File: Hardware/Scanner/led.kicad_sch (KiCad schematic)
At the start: 20 parts, among them U5 TLC59208FIPWR

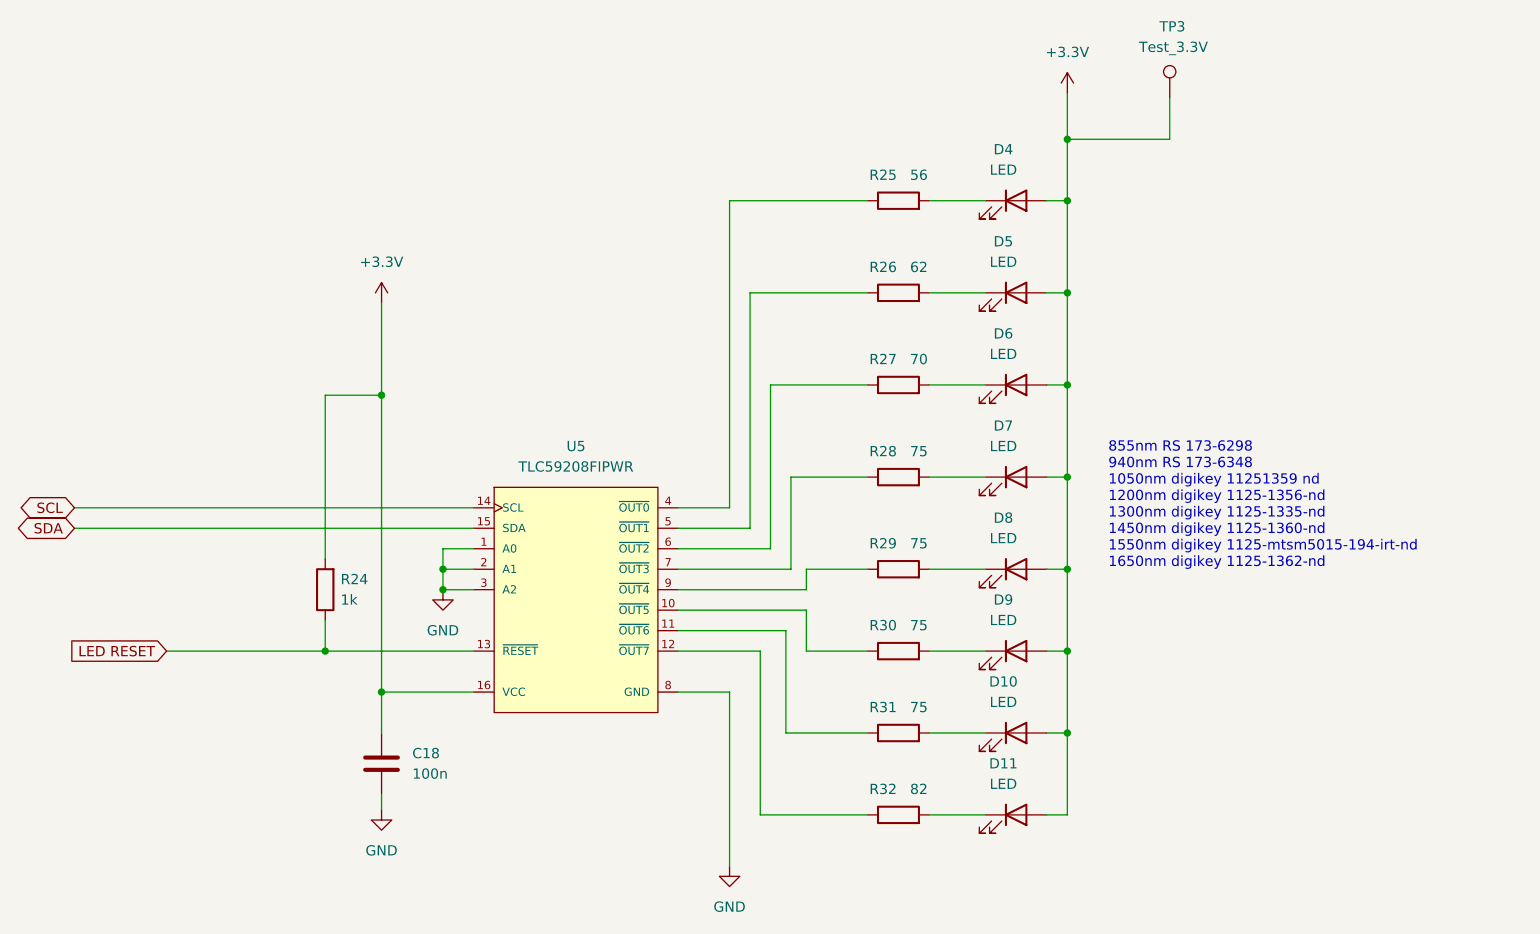
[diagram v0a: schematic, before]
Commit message: Updated LED and crystal descriptions
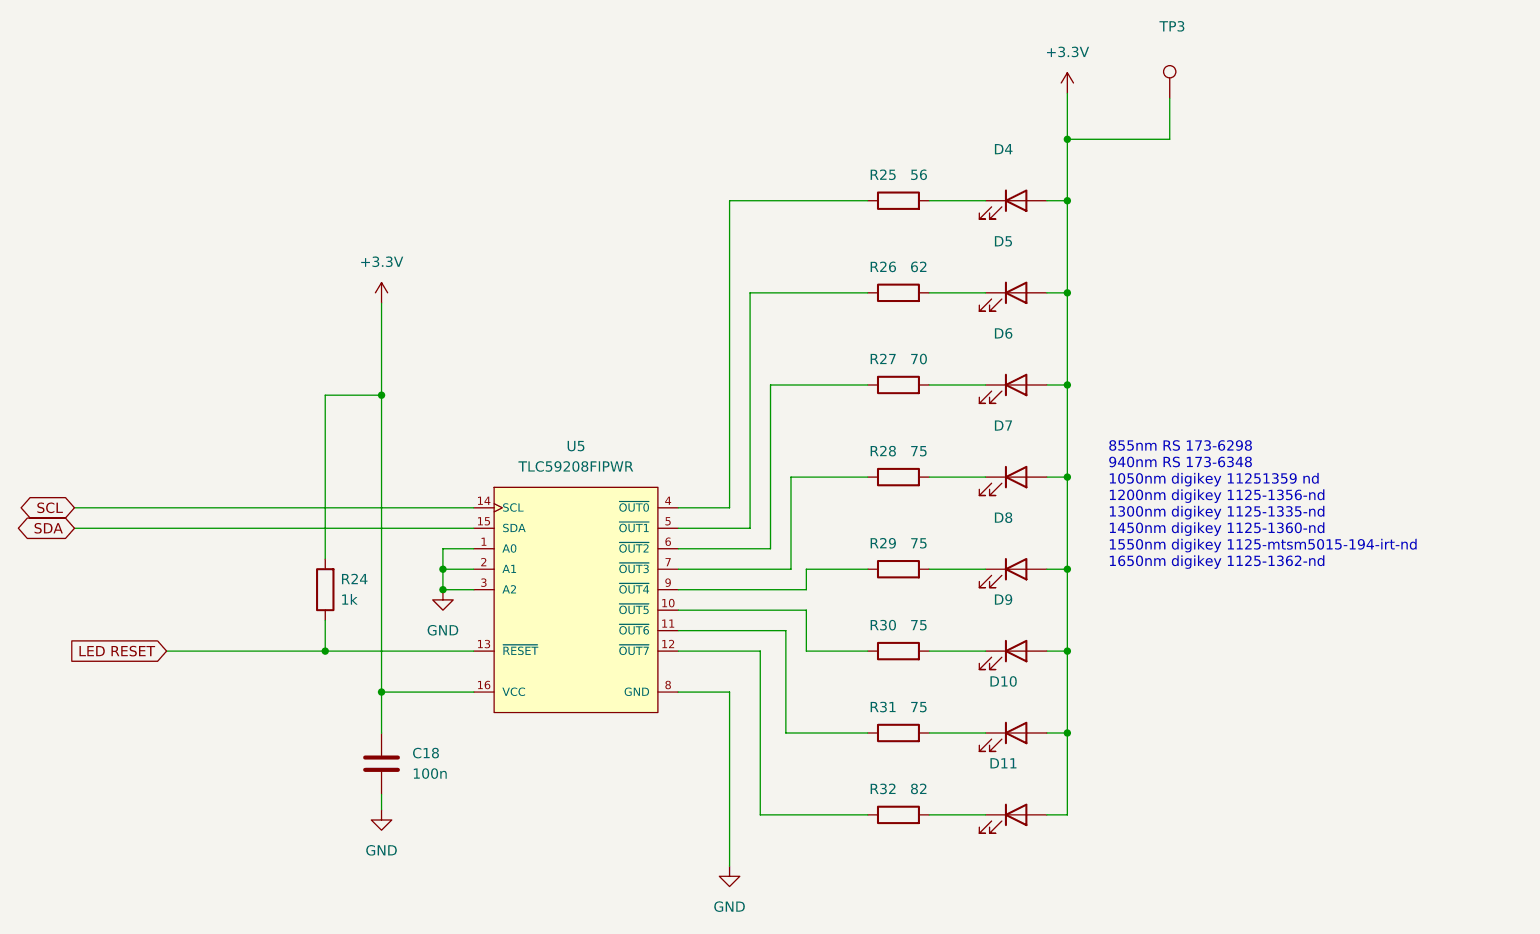
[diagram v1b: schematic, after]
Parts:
- D10, D11, D4, D5, D6, D7, D8, D9: value LED -> (none); footprint LED_SMD:LED_1206_3216Metric_Pad1.42x1.75mm_HandSolder -> (none)
- TP3: value Test_3.3V -> (none); footprint TestPoint:TestPoint_Pad_D1.5mm -> (none); now left out of the parts list
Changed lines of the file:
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@@
     (in_bom yes) (on_board yes) (fields_autoplaced)
     (property "Reference" "D8" (id 0) (at 200.3425 93.98 0))
-    (property "Value" "LED" (id 1) (at 200.3425 96.52 0))
-    (property "Footprint" "LED_SMD:LED_1206_3216Metric_Pad1.42x1.75mm_HandSolder" (id 2) (at 201.93 100.33 0)
+    (property "Value" "" (id 1) (at 200.3425 96.52 0))
+    (property "Footprint" "" (id 2) (at 201.93 100.33 0)
       (effects (font (size 1.27 1.27)) hide)
     )
@@
   )
   (symbol (lib_id "Connector:TestPoint") (at 220.98 41.91 0) (unit 1)
-    (in_bom yes) (on_board yes)
+    (in_bom no) (on_board yes)
     (property "Reference" "TP3" (id 0) (at 219.71 33.02 0)
       (effects (font (size 1.27 1.27)) (justify left))
     )
-    (property "Value" "Test_3.3V" (id 1) (at 217.17 35.56 0)
+    (property "Value" "" (id 1) (at 217.17 35.56 0)
       (effects (font (size 1.27 1.27)) (justify left))
     )
-    (property "Footprint" "TestPoint:TestPoint_Pad_D1.5mm" (id 2) (at 226.06 41.91 0)
+    (property "Footprint" "" (id 2) (at 226.06 41.91 0)
       (effects (font (size 1.27 1.27)) hide)
     )
@@
     (in_bom yes) (on_board yes) (fields_autoplaced)
     (property "Reference" "D9" (id 0) (at 200.3425 104.14 0))
-    (property "Value" "LED" (id 1) (at 200.3425 106.68 0))
-    (property "Footprint" "LED_SMD:LED_1206_3216Metric_Pad1.42x1.75mm_HandSolder" (id 2) (at 201.93 110.49 0)
+    (property "Value" "" (id 1) (at 200.3425 106.68 0))
+    (property "Footprint" "" (id 2) (at 201.93 110.49 0)
       (effects (font (size 1.27 1.27)) hide)
     )
@@
     (in_bom yes) (on_board yes) (fields_autoplaced)
     (property "Reference" "D4" (id 0) (at 200.3425 48.26 0))
-    (property "Value" "LED" (id 1) (at 200.3425 50.8 0))
-    (property "Footprint" "LED_SMD:LED_1206_3216Metric_Pad1.42x1.75mm_HandSolder" (id 2) (at 201.93 54.61 0)
+    (property "Value" "" (id 1) (at 200.3425 50.8 0))
+    (property "Footprint" "" (id 2) (at 201.93 54.61 0)
       (effects (font (size 1.27 1.27)) hide)
     )
@@
     (in_bom yes) (on_board yes) (fields_autoplaced)
     (property "Reference" "D7" (id 0) (at 200.3425 82.55 0))
-    (property "Value" "LED" (id 1) (at 200.3425 85.09 0))
-    (property "Footprint" "LED_SMD:LED_1206_3216Metric_Pad1.42x1.75mm_HandSolder" (id 2) (at 201.93 88.9 0)
+    (property "Value" "" (id 1) (at 200.3425 85.09 0))
+    (property "Footprint" "" (id 2) (at 201.93 88.9 0)
       (effects (font (size 1.27 1.27)) hide)
     )
@@
     (in_bom yes) (on_board yes) (fields_autoplaced)
     (property "Reference" "D11" (id 0) (at 200.3425 124.46 0))
-    (property "Value" "LED" (id 1) (at 200.3425 127 0))
-    (property "Footprint" "LED_SMD:LED_1206_3216Metric_Pad1.42x1.75mm_HandSolder" (id 2) (at 201.93 130.81 0)
+    (property "Value" "" (id 1) (at 200.3425 127 0))
+    (property "Footprint" "" (id 2) (at 201.93 130.81 0)
       (effects (font (size 1.27 1.27)) hide)
     )
@@
     (in_bom yes) (on_board yes) (fields_autoplaced)
     (property "Reference" "D6" (id 0) (at 200.3425 71.12 0))
-    (property "Value" "LED" (id 1) (at 200.3425 73.66 0))
-    (property "Footprint" "LED_SMD:LED_1206_3216Metric_Pad1.42x1.75mm_HandSolder" (id 2) (at 201.93 77.47 0)
+    (property "Value" "" (id 1) (at 200.3425 73.66 0))
+    (property "Footprint" "" (id 2) (at 201.93 77.47 0)
       (effects (font (size 1.27 1.27)) hide)
     )
@@
     (in_bom yes) (on_board yes) (fields_autoplaced)
     (property "Reference" "D5" (id 0) (at 200.3425 59.69 0))
-    (property "Value" "LED" (id 1) (at 200.3425 62.23 0))
-    (property "Footprint" "LED_SMD:LED_1206_3216Metric_Pad1.42x1.75mm_HandSolder" (id 2) (at 201.93 66.04 0)
+    (property "Value" "" (id 1) (at 200.3425 62.23 0))
+    (property "Footprint" "" (id 2) (at 201.93 66.04 0)
       (effects (font (size 1.27 1.27)) hide)
     )
@@
     (in_bom yes) (on_board yes) (fields_autoplaced)
     (property "Reference" "D10" (id 0) (at 200.3425 114.3 0))
-    (property "Value" "LED" (id 1) (at 200.3425 116.84 0))
-    (property "Footprint" "LED_SMD:LED_1206_3216Metric_Pad1.42x1.75mm_HandSolder" (id 2) (at 201.93 120.65 0)
-      (effects (font (size 1.27 1.27)) hide)
-    )
+    (property "Value" "" (id 1) (at 200.3425 116.84 0))
+    (property "Footprint" "" (id 2) (at 201.93 120.65 0)
+      (effects (font (size 1.27 1.27)) hide)
+    )

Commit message: Consistency of capacitor values
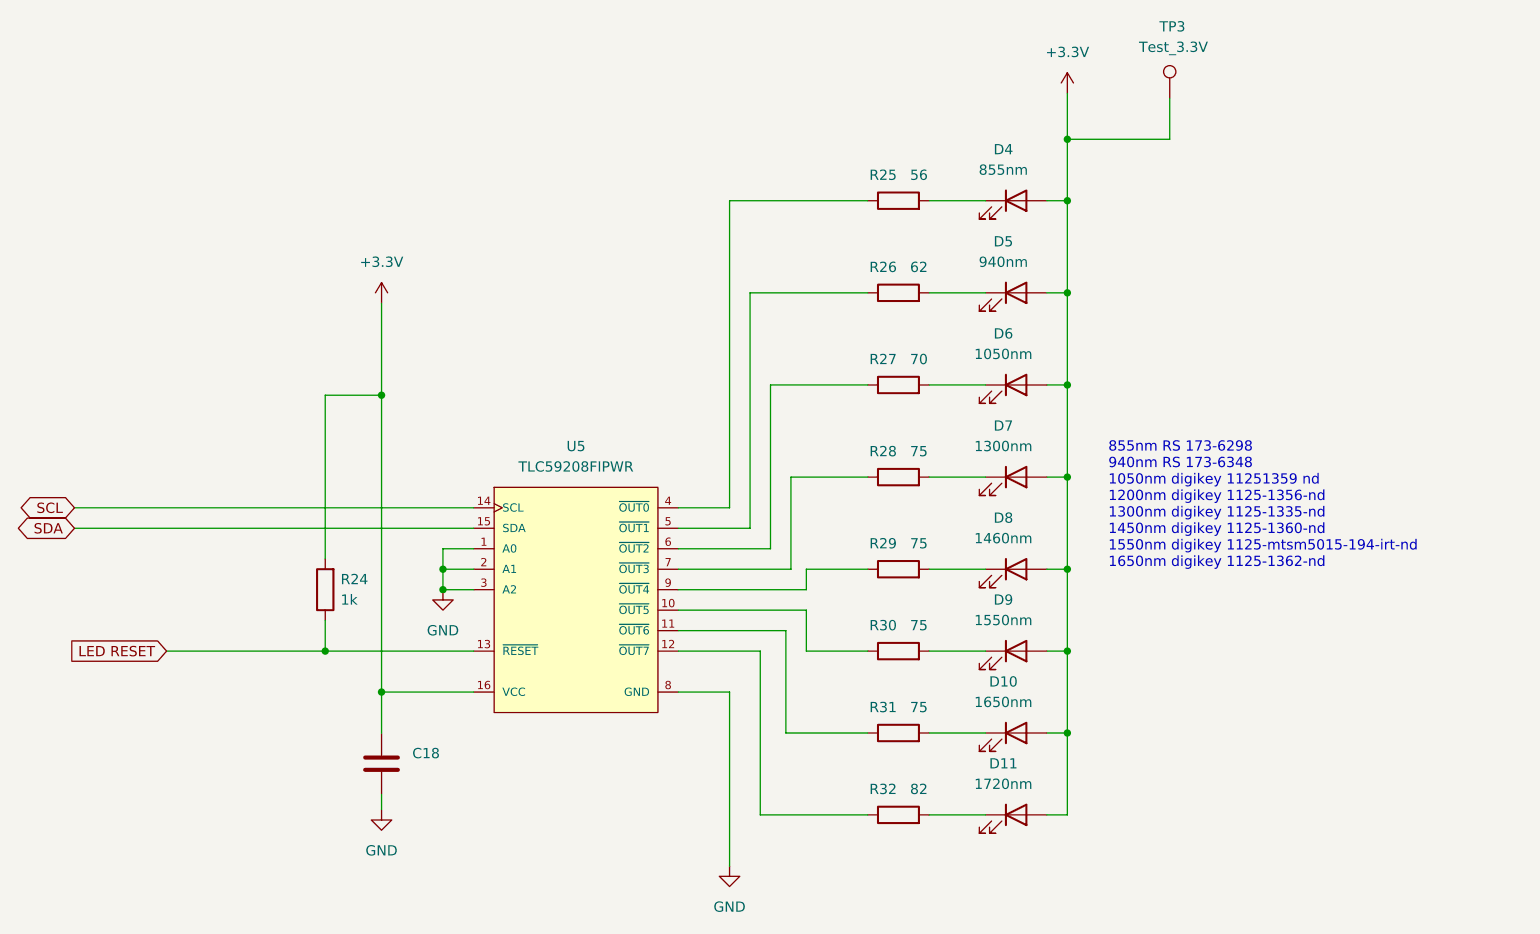
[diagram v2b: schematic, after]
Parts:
- C18: value 100n -> (none)
- D10: value (none) -> 1650nm; footprint (none) -> LED_SMD:LED_1206_3216Metric_Pad1.42x1.75mm_HandSolder
- D11: value (none) -> 1720nm; footprint (none) -> LED_SMD:LED_1206_3216Metric_Pad1.42x1.75mm_HandSolder
- D4: value (none) -> 855nm; footprint (none) -> LED_SMD:LED_1206_3216Metric_Pad1.42x1.75mm_HandSolder
- D5: value (none) -> 940nm; footprint (none) -> LED_SMD:LED_1206_3216Metric_Pad1.42x1.75mm_HandSolder
- D6: value (none) -> 1050nm; footprint (none) -> LED_SMD:LED_1206_3216Metric_Pad1.42x1.75mm_HandSolder
- D7: value (none) -> 1300nm; footprint (none) -> LED_SMD:LED_1206_3216Metric_Pad1.42x1.75mm_HandSolder
- D8: value (none) -> 1460nm; footprint (none) -> LED_SMD:LED_1206_3216Metric_Pad1.42x1.75mm_HandSolder
- D9: value (none) -> 1550nm; footprint (none) -> LED_SMD:LED_1206_3216Metric_Pad1.42x1.75mm_HandSolder
- TP3: value (none) -> Test_3.3V; footprint (none) -> TestPoint:TestPoint_Pad_D1.5mm
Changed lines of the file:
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@@
     (in_bom yes) (on_board yes) (fields_autoplaced)
     (property "Reference" "D8" (id 0) (at 200.3425 93.98 0))
-    (property "Value" "" (id 1) (at 200.3425 96.52 0))
-    (property "Footprint" "" (id 2) (at 201.93 100.33 0)
+    (property "Value" "1460nm" (id 1) (at 200.3425 96.52 0))
+    (property "Footprint" "LED_SMD:LED_1206_3216Metric_Pad1.42x1.75mm_HandSolder" (id 2) (at 201.93 100.33 0)
       (effects (font (size 1.27 1.27)) hide)
     )
@@
       (effects (font (size 1.27 1.27)) (justify left))
     )
-    (property "Value" "" (id 1) (at 217.17 35.56 0)
+    (property "Value" "Test_3.3V" (id 1) (at 217.17 35.56 0)
       (effects (font (size 1.27 1.27)) (justify left))
     )
-    (property "Footprint" "" (id 2) (at 226.06 41.91 0)
+    (property "Footprint" "TestPoint:TestPoint_Pad_D1.5mm" (id 2) (at 226.06 41.91 0)
       (effects (font (size 1.27 1.27)) hide)
     )
@@
       (effects (font (size 1.27 1.27)) (justify left))
     )
-    (property "Value" "100n" (id 1) (at 127 125.7299 0)
+    (property "Value" "" (id 1) (at 127 125.7299 0)
       (effects (font (size 1.27 1.27)) (justify left))
     )
@@
     (in_bom yes) (on_board yes) (fields_autoplaced)
     (property "Reference" "D9" (id 0) (at 200.3425 104.14 0))
-    (property "Value" "" (id 1) (at 200.3425 106.68 0))
-    (property "Footprint" "" (id 2) (at 201.93 110.49 0)
+    (property "Value" "1550nm" (id 1) (at 200.3425 106.68 0))
+    (property "Footprint" "LED_SMD:LED_1206_3216Metric_Pad1.42x1.75mm_HandSolder" (id 2) (at 201.93 110.49 0)
       (effects (font (size 1.27 1.27)) hide)
     )
@@
     (in_bom yes) (on_board yes) (fields_autoplaced)
     (property "Reference" "D4" (id 0) (at 200.3425 48.26 0))
-    (property "Value" "" (id 1) (at 200.3425 50.8 0))
-    (property "Footprint" "" (id 2) (at 201.93 54.61 0)
+    (property "Value" "855nm " (id 1) (at 200.3425 50.8 0))
+    (property "Footprint" "LED_SMD:LED_1206_3216Metric_Pad1.42x1.75mm_HandSolder" (id 2) (at 201.93 54.61 0)
       (effects (font (size 1.27 1.27)) hide)
     )
@@
     (in_bom yes) (on_board yes) (fields_autoplaced)
     (property "Reference" "D7" (id 0) (at 200.3425 82.55 0))
-    (property "Value" "" (id 1) (at 200.3425 85.09 0))
-    (property "Footprint" "" (id 2) (at 201.93 88.9 0)
+    (property "Value" "1300nm" (id 1) (at 200.3425 85.09 0))
+    (property "Footprint" "LED_SMD:LED_1206_3216Metric_Pad1.42x1.75mm_HandSolder" (id 2) (at 201.93 88.9 0)
       (effects (font (size 1.27 1.27)) hide)
     )
@@
     (in_bom yes) (on_board yes) (fields_autoplaced)
     (property "Reference" "D11" (id 0) (at 200.3425 124.46 0))
-    (property "Value" "" (id 1) (at 200.3425 127 0))
-    (property "Footprint" "" (id 2) (at 201.93 130.81 0)
+    (property "Value" "1720nm" (id 1) (at 200.3425 127 0))
+    (property "Footprint" "LED_SMD:LED_1206_3216Metric_Pad1.42x1.75mm_HandSolder" (id 2) (at 201.93 130.81 0)
       (effects (font (size 1.27 1.27)) hide)
     )
@@
     (in_bom yes) (on_board yes) (fields_autoplaced)
     (property "Reference" "D6" (id 0) (at 200.3425 71.12 0))
-    (property "Value" "" (id 1) (at 200.3425 73.66 0))
-    (property "Footprint" "" (id 2) (at 201.93 77.47 0)
+    (property "Value" "1050nm" (id 1) (at 200.3425 73.66 0))
+    (property "Footprint" "LED_SMD:LED_1206_3216Metric_Pad1.42x1.75mm_HandSolder" (id 2) (at 201.93 77.47 0)
       (effects (font (size 1.27 1.27)) hide)
     )
@@
     (in_bom yes) (on_board yes) (fields_autoplaced)
     (property "Reference" "D5" (id 0) (at 200.3425 59.69 0))
-    (property "Value" "" (id 1) (at 200.3425 62.23 0))
-    (property "Footprint" "" (id 2) (at 201.93 66.04 0)
+    (property "Value" "940nm" (id 1) (at 200.3425 62.23 0))
+    (property "Footprint" "LED_SMD:LED_1206_3216Metric_Pad1.42x1.75mm_HandSolder" (id 2) (at 201.93 66.04 0)
       (effects (font (size 1.27 1.27)) hide)
     )
@@
     (in_bom yes) (on_board yes) (fields_autoplaced)
     (property "Reference" "D10" (id 0) (at 200.3425 114.3 0))
-    (property "Value" "" (id 1) (at 200.3425 116.84 0))
-    (property "Footprint" "" (id 2) (at 201.93 120.65 0)
-      (effects (font (size 1.27 1.27)) hide)
-    )
+    (property "Value" "1650nm" (id 1) (at 200.3425 116.84 0))
+    (property "Footprint" "LED_SMD:LED_1206_3216Metric_Pad1.42x1.75mm_HandSolder" (id 2) (at 201.93 120.65 0)
+      (effects (font (size 1.27 1.27)) hide)
+    )
